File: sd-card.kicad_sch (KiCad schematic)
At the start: 6 parts, among them J1 Micro_SD_Card_Det_Hirose_DM3AT

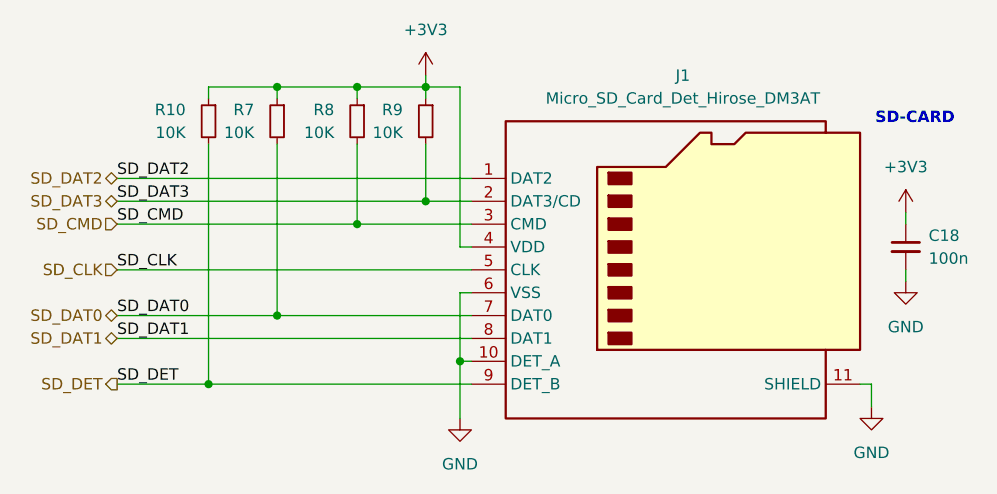
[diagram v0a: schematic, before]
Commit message: Finished SDRAM, LTDC, QSPI, SDMMC, still an error on LTDC B channel
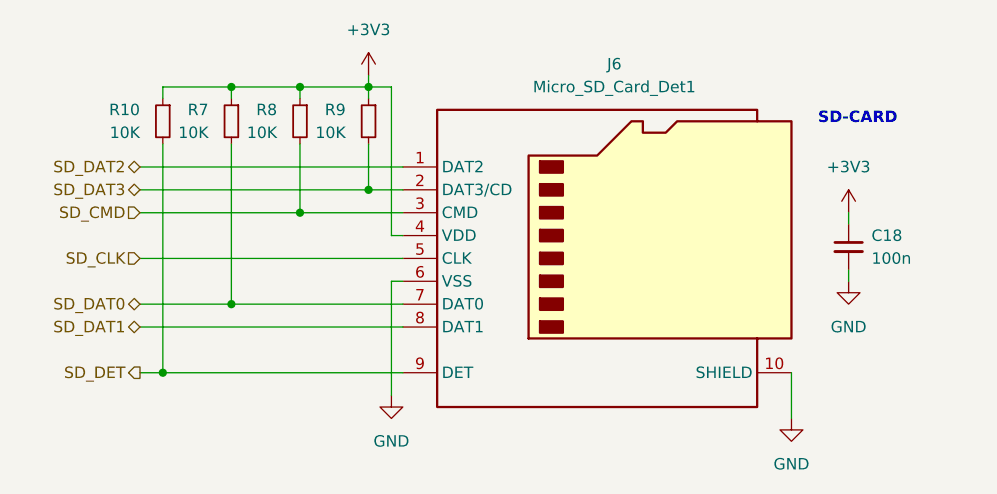
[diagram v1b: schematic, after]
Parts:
- removed J1: Micro_SD_Card_Det_Hirose_DM3AT, Connector_Card:microSD_HC_Hirose_DM3AT-SF-PEJM5, symbol Connector:Micro_SD_Card_Det_Hirose_DM3AT
- added J6: Micro_SD_Card_Det1, TF-115:SD-TF-115, symbol Connector:Micro_SD_Card_Det1
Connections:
- net +3V3: now also J6.4 (VDD)
- net GND: now also J6.10 (SHIELD), J6.6 (VSS)
- net SD_CLK: now also J6.5 (CLK)
- net SD_CMD: now also J6.3 (CMD)
- net SD_DAT0: now also J6.7 (DAT0)
- net SD_DAT1: now also J6.8 (DAT1)
- net SD_DAT2: now also J6.1 (DAT2)
- net SD_DAT3: now also J6.2 (DAT3/CD)
- net SD_DET: now also J6.9 (DET)
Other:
- moved on the sheet: C18, R10, R7, R8, R9
